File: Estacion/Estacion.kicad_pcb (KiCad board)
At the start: 2 copper layers, 5 parts, among them U1 FN-M16P, U2 RP2040-ZERO, U3 DHT22

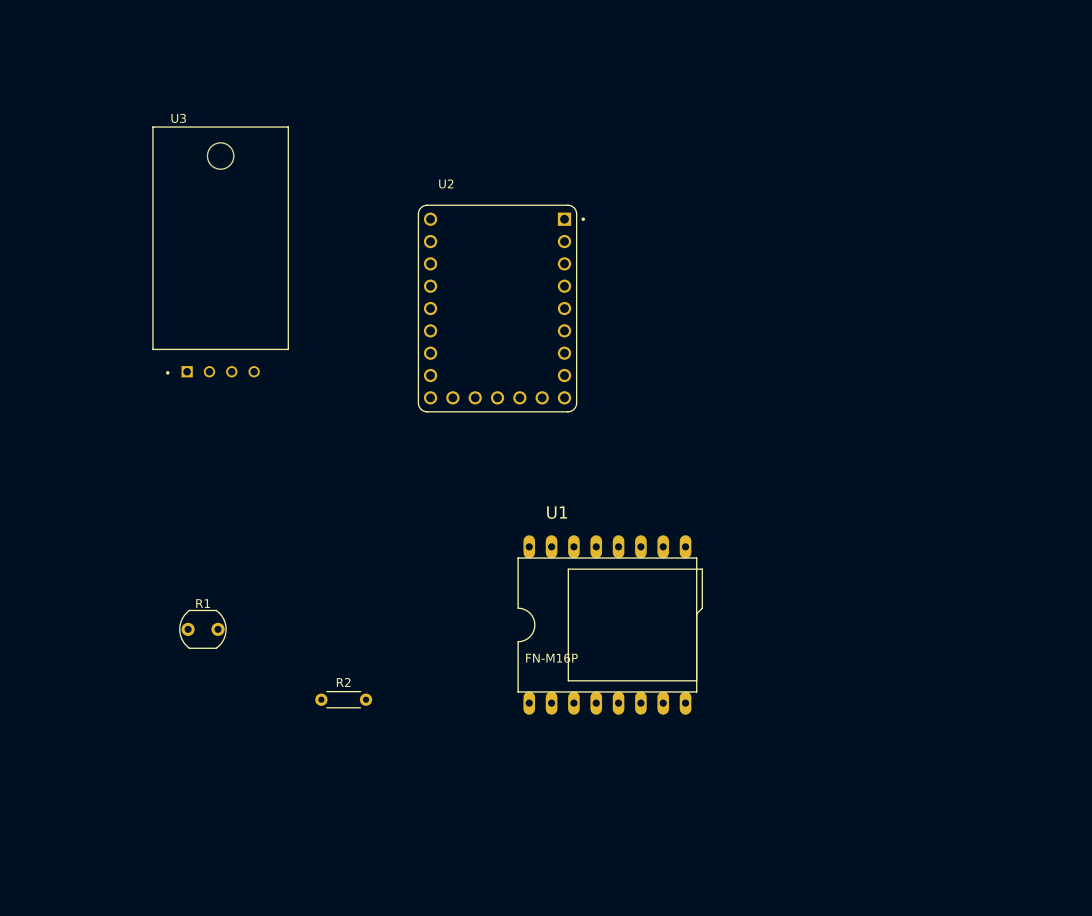
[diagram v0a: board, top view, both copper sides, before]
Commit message: preparaciones
Relacionar footprints con modelados 3d, delimitar espacio de pcb, retocar conexiones y asegurar cumplimiento de ERC
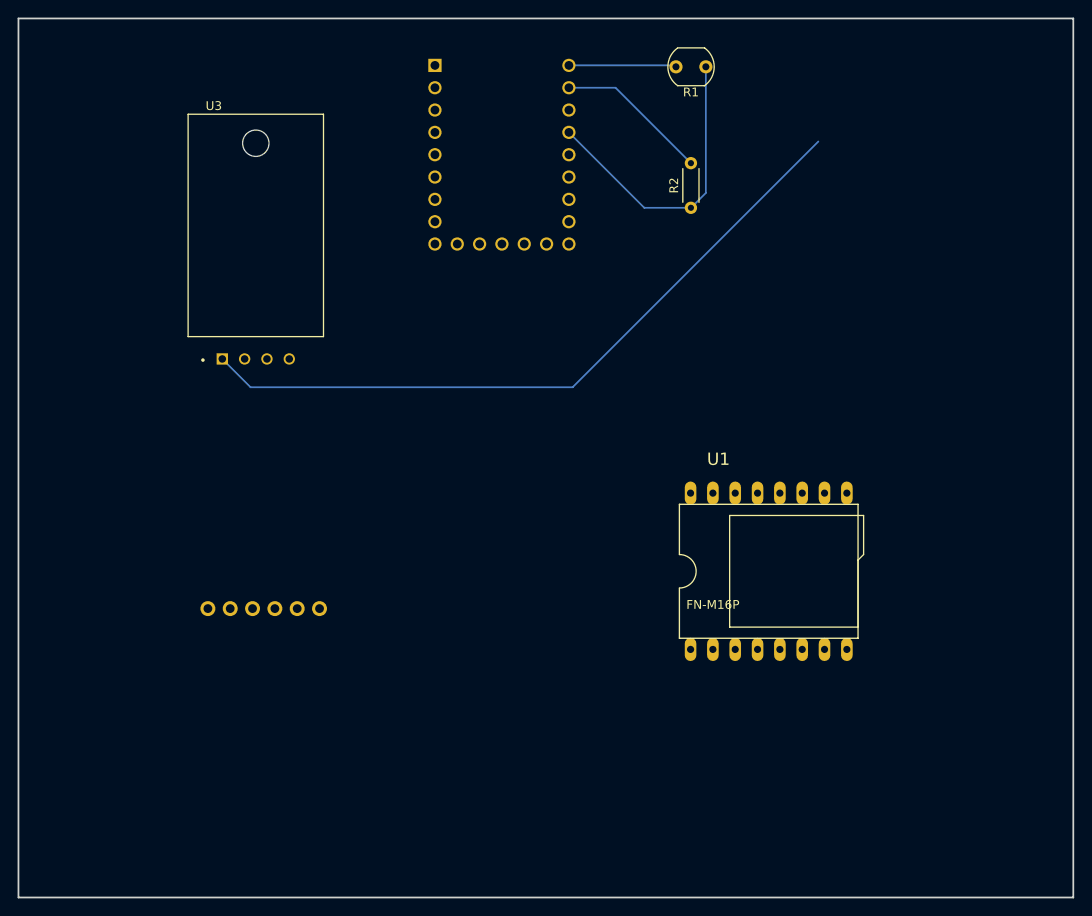
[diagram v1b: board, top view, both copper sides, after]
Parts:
- added BMP280: BMP18, especificos:BMP180, F.Cu at (99.3, 119.1)
- U2: moved to B.Cu
- moved R1 87.0 mm to (143.2, 57.5), turned to 180 degrees
- moved R2 70.0 mm to (141.5, 73.5), turned to 90 degrees
- moved U1 19.3 mm to (150.3, 114.9)
- moved U2 17.5 mm to (120.0, 67.5), turned to 180 degrees
- moved U3 4.26 mm to (92.0, 75.5)
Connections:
- R1 pad 1: unconnected-(R1-Pad1) -> Net-(U2-GP29)
- R1 pad 2: unconnected-(R1-Pad2) -> Net-(U2-5V)
- R2 pad 1: unconnected-(R2-Pad1) -> Net-(U2-GP29)
- R2 pad 2: unconnected-(R2-Pad2) -> GND
- U1 pad 1: unconnected-(U1-VCC-Pad1) -> Net-(BMP280-VCC)
- U1 pad 10: unconnected-(U1-GND-Pad10) -> GND
- U1 pad 2: unconnected-(U1-RX-Pad2) -> Net-(U1-RX)
- U1 pad 3: unconnected-(U1-TX-Pad3) -> Net-(U1-TX)
- U1 pad 6: unconnected-(U1-SPK+-Pad6) -> Net-(U1-SPK+)
- U1 pad 8: unconnected-(U1-SPK--Pad8) -> Net-(U1-SPK-)
- U2 pad 10: unconnected-(U2-GP9-Pad10) -> Net-(U2-GP9)
- U2 pad 12: unconnected-(U2-GP11-Pad12) -> Net-(U1-RX)
- U2 pad 13: unconnected-(U2-GP12-Pad13) -> Net-(U1-TX)
- U2 pad 17: unconnected-(U2-GP26-Pad17) -> Net-(BMP280-SDA)
- U2 pad 18: unconnected-(U2-GP27-Pad18) -> Net-(BMP280-SCL)
- U2 pad 20: unconnected-(U2-GP29-Pad20) -> Net-(U2-GP29)
- U2 pad 21: unconnected-(U2-3V3-Pad21) -> Net-(BMP280-VCC)
- U2 pad 22: unconnected-(U2-GND-Pad22) -> GND
- U2 pad 23: unconnected-(U2-5V-Pad23) -> Net-(U2-5V)
- U3 pad 1: unconnected-(U3-VDD-Pad1) -> Net-(BMP280-VCC)
- U3 pad 2: unconnected-(U3-DATA-Pad2) -> Net-(U2-GP9)
- U3 pad 4: unconnected-(U3-GND-Pad4) -> GND
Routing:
- net Net-(BMP280-VCC): track 0.00 -> 80.7 mm
- net Net-(U2-GP29): track 0.00 -> 34.2 mm
- net GND: track 0.00 -> 17.4 mm
- net Net-(U2-5V): track 0.00 -> 12.2 mm
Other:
- board outline added: 120 x 100 mm

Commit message: Wemos s2 mini
Se cambia el controlador y se realizan las conexiones en el diagrama
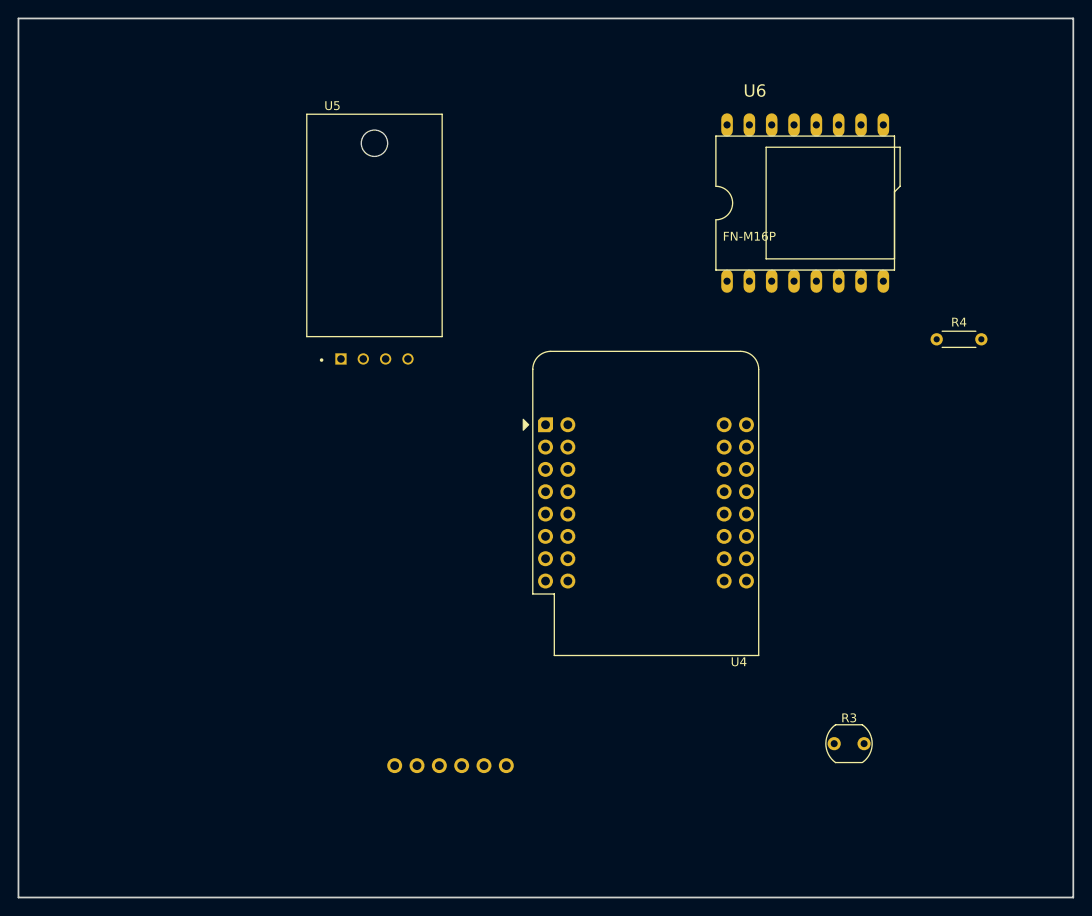
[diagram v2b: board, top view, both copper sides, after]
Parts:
- removed R1: LDR07, OptoDevice:R_LDR_5.1x4.3mm_P3.4mm_Vertical
- removed R2: R_US, Resistor_THT:R_Axial_DIN0204_L3.6mm_D1.6mm_P5.08mm_Horizontal
- removed U1: FN-M16P, especificos:FN-M16P
- removed U2: RP2040-ZERO, especificos:MODULE_RP2040-ZERO
- removed U3: DHT22, especificos:XDCR_DHT22
- added R3: LDR07, OptoDevice:R_LDR_5.1x4.3mm_P3.4mm_Vertical, F.Cu at (157.8, 134.5)
- added R4: R_US, Resistor_THT:R_Axial_DIN0204_L3.6mm_D1.6mm_P5.08mm_Horizontal, F.Cu at (169.5, 88.5)
- added U4: WeMos_S2_mini, especificos:WEMOS_S2_mini, F.Cu at (125.0, 98.2)
- added U5: DHT22, especificos:XDCR_DHT22, F.Cu at (105.5, 75.5)
- added U6: FN-M16P, especificos:FN-M16P, F.Cu at (154.5, 73.0)
- moved BMP280 27.8 mm to (120.5, 137.0)
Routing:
- net Net-(BMP280-VCC): track 80.7 -> 0.00 mm
- net Net-(U2-GP29): track 34.2 -> 0.00 mm
- net GND: track 17.4 -> 0.00 mm
- net Net-(U2-5V): track 12.2 -> 0.00 mm

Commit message: .
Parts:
- moved R4 44.3 mm to (146.0, 126.0)
- moved U4 21.1 mm to (145.9, 96.1), turned to -90 degrees
- moved U5 15.6 mm to (95.5, 87.5)
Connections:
- R3 pad 2: Net-(U4-GPIO3) -> Net-(U4-GPIO39)
- R4 pad 2: Net-(U4-GPIO3) -> Net-(U4-GPIO39)
- U4 pad 16: unconnected-(U4-GPIO39-Pad16) -> Net-(U4-GPIO39)
- U4 pad 2: Net-(U4-GPIO3) -> unconnected-(U4-GPIO3-Pad2)
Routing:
- net Net-(U4-GPIO21): track 0.00 -> 47.2 mm, vias 0 -> 2
- net Net-(BMP280-SCL): track 0.00 -> 44.7 mm
- net Net-(BMP280-SDA): track 0.00 -> 44.7 mm
- net Net-(U4-GPIO2): track 0.00 -> 30.7 mm
- net Net-(U4-GPIO1): track 0.00 -> 17.7 mm
- net Net-(BMP280-VCC): track 0.00 -> 1.99 mm
- net unconnected-(U4-GPIO3-Pad2): track 0.00 -> 0.52 mm
- added copper zone on B.Cu, net GND
